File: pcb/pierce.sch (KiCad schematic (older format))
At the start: 49 parts, among them J3 Trackpoint, SW1 SW_PUSH, SW10 SW_PUSH, SW14 SW_PUSH, SW18 SW_PUSH, SW2 SW_PUSH, SW22 SW_PUSH, SW26 SW_PUSH, SW3 SW_PUSH, SW33 SW_PUSH, SW37 SW_PUSH, SW4 SW_PUSH, SW5 SW_PUSH, SW6 SW_PUSH, SW7 SW_PUSH, SW8 SW_PUSH, SW9 SW_PUSH, U1 Elite-C_reverse

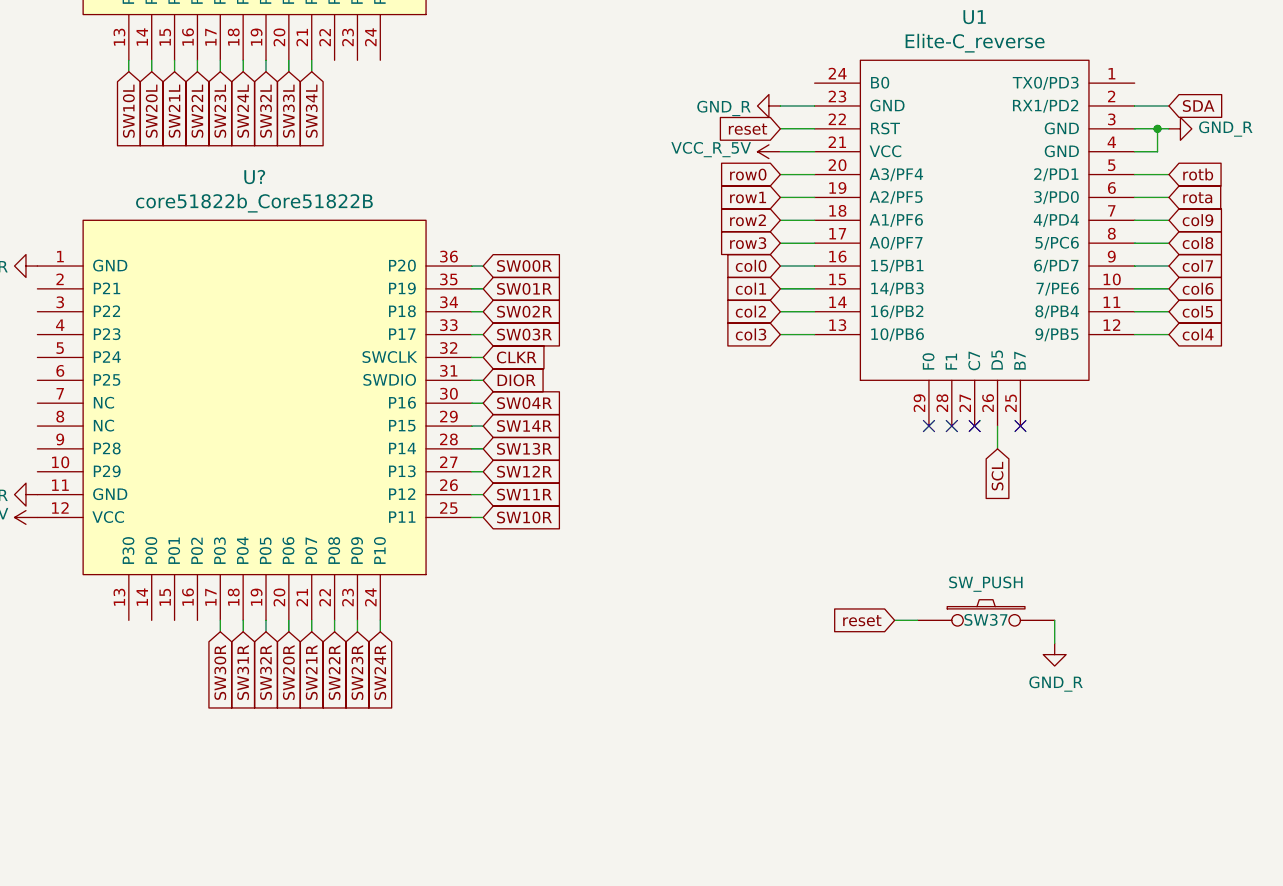
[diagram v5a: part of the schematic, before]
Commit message: adjust schematics with i2c connecion to elite-c
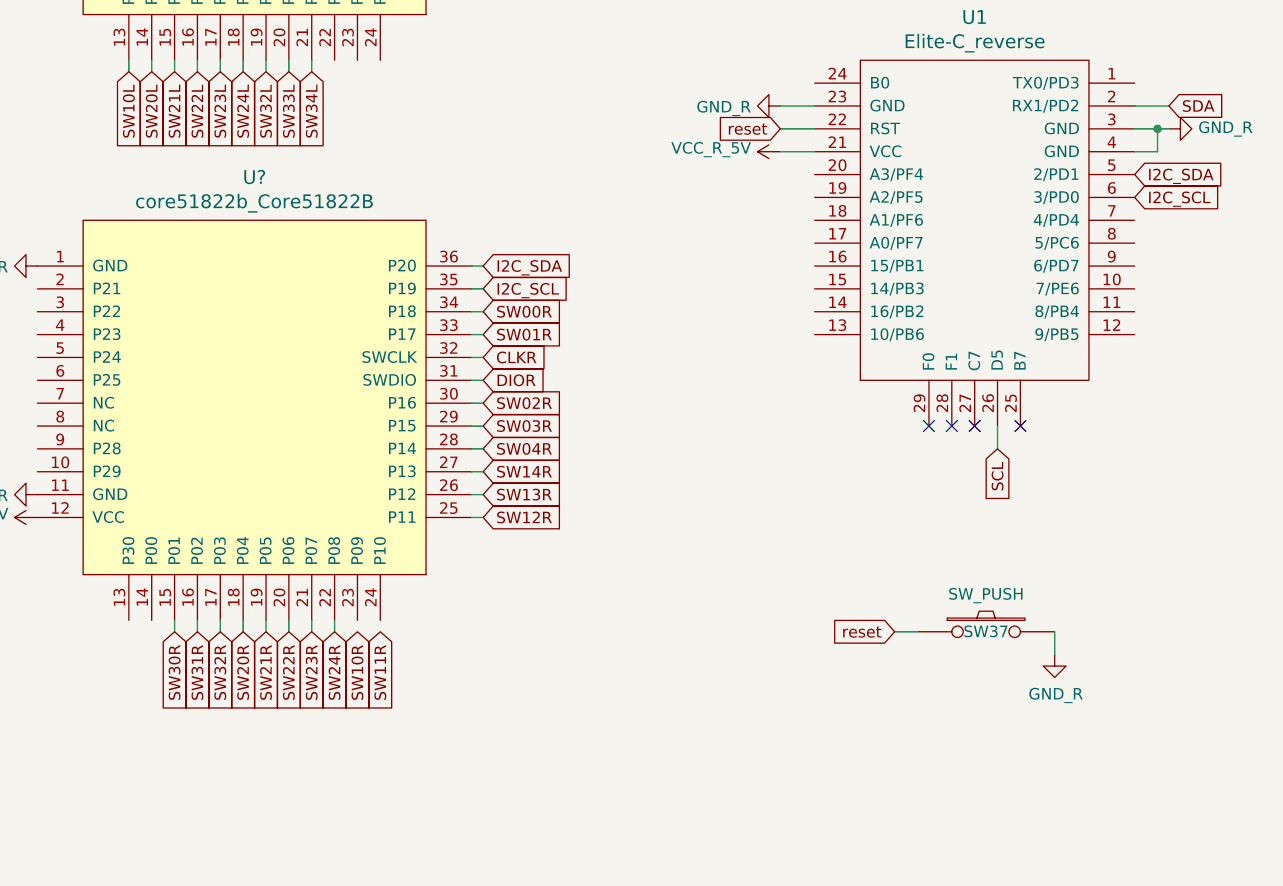
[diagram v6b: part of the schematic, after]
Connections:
- net SW00R: now also U?.34 (P18); no longer U?.36 (P20)
- net SW01R: now also U?.33 (P17); no longer U?.35 (P19)
- net SW02R: now also U?.30 (P16); no longer U?.34 (P18)
- net SW03R: now also U?.29 (P15); no longer U?.33 (P17)
- net SW04R: now also U?.28 (P14); no longer U?.30 (P16)
- net SW10R: no longer U?.25 (P11)
- net SW11R: no longer U?.26 (P12)
- net SW12R: now also U?.25 (P11); no longer U?.27 (P13)
- net SW13R: now also U?.26 (P12); no longer U?.28 (P14)
- net SW14R: now also U?.27 (P13); no longer U?.29 (P15)
- net SW20R: now also U?.18 (P04); no longer U?.20 (P06)
- net SW21R: now also U?.19 (P05); no longer U?.21 (P07)
- net SW22R: now also U?.20 (P06); no longer U?.22 (P08)
- net SW23R: now also U?.21 (P07); no longer U?.23 (P09)
- net SW24R: now also U?.22 (P08); no longer U?.24 (P10)
- net SW30R: now also U?.15 (P01); no longer U?.17 (P03)
- net SW31R: now also U?.16 (P02); no longer U?.18 (P04)
- net SW32R: now also U?.17 (P03); no longer U?.19 (P05)
- net col0: no longer names the net of U1.16 (15/PB1)
- net col1: no longer names the net of U1.15 (14/PB3)
- net col2: no longer names the net of U1.14 (16/PB2)
- net col3: no longer names the net of U1.13 (10/PB6)
- net col4: no longer names the net of U1.12 (9/PB5)
- net col5: no longer names the net of U1.11 (8/PB4)
- net col6: no longer names the net of U1.10 (7/PE6)
- net col7: no longer names the net of U1.9 (6/PD7)
- net col8: no longer names the net of U1.8 (5/PC6)
- net col9: no longer names the net of U1.7 (4/PD4)
- net rota renamed I2C_SCL
- net I2C_SCL: now also U?.35 (P19)
- net rotb renamed I2C_SDA
- net I2C_SDA: now also U?.36 (P20)
- net row0: no longer names the net of U1.20 (A3/PF4)
- net row1: no longer names the net of U1.19 (A2/PF5)
- net row2: no longer names the net of U1.18 (A1/PF6)
- net row3: no longer names the net of U1.17 (A0/PF7)
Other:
- moved on the sheet: SW37
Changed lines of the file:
@@
 Wire Wire Line
 	10700 3250 10750 3250
-Text GLabel 10750 4150 2    50   Input ~ 0
-col4
-Text GLabel 10750 4050 2    50   Input ~ 0
-col5
-Text GLabel 10750 3950 2    50   Input ~ 0
-col6
-Text GLabel 10750 3850 2    50   Input ~ 0
-col7
-Text GLabel 10750 3750 2    50   Input ~ 0
-col8
-Text GLabel 10750 3650 2    50   Input ~ 0
-col9
-Wire Wire Line
-	10600 3650 10750 3650
-Wire Wire Line
-	10600 3750 10750 3750
-Wire Wire Line
-	10600 3850 10750 3850
-Wire Wire Line
-	10600 3950 10750 3950
-Wire Wire Line
-	10600 4050 10750 4050
-Wire Wire Line
-	10600 4150 10750 4150
-$Comp
-L pierce:SW_PUSH SW37
-U 1 1 60617B11
-P 9950 5400
-F 0 "SW37" H 9950 5400 50  0000 C CNN
-F 1 "SW_PUSH" H 9950 5564 50  0000 C CNN
-F 2 "kbd:ResetSW_1side" H 9950 5400 50  0001 C CNN
-F 3 "" H 9950 5400 50  0000 C CNN
-	1    9950 5400
-	1    0    0    -1
-$EndComp
-Text GLabel 9550 5400 0    50   Input ~ 0
-reset
-Wire Wire Line
-	9550 5400 9650 5400
-Wire Wire Line
-	10250 5500 10250 5400
 $Comp
 L Device:R R2
@@
 Wire Wire Line
 	9200 3250 9050 3250
-Text GLabel 9050 3450 0    50   Input ~ 0
-row0
-Text GLabel 9050 3550 0    50   Input ~ 0
-row1
-Text GLabel 9050 3650 0    50   Input ~ 0
-row2
-Text GLabel 9050 3750 0    50   Input ~ 0
-row3
-Text GLabel 9050 3850 0    50   Input ~ 0
-col0
-Text GLabel 9050 3950 0    50   Input ~ 0
-col1
-Text GLabel 9050 4050 0    50   Input ~ 0
-col2
-Text GLabel 9050 4150 0    50   Input ~ 0
-col3
-Wire Wire Line
-	9050 3450 9200 3450
-Wire Wire Line
-	9050 3550 9200 3550
-Wire Wire Line
-	9050 3650 9200 3650
-Wire Wire Line
-	9050 3750 9200 3750
-Wire Wire Line
-	9050 3850 9200 3850
-Wire Wire Line
-	9050 3950 9200 3950
-Wire Wire Line
-	9050 4050 9200 4050
-Wire Wire Line
-	9050 4150 9200 4150
 Wire Wire Line
 	9200 3350 9050 3350
@@
 Wire Wire Line
 	9500 1250 9500 1900
-Text GLabel 10750 3550 2    50   Input ~ 0
-rota
-Text GLabel 10750 3450 2    50   Input ~ 0
-rotb
-Wire Wire Line
-	10750 3450 10600 3450
-Wire Wire Line
-	10750 3550 10600 3550
 $Comp
 L pierce:SW_PUSH SW22
@@
 Wire Wire Line
 	5100 5100 5100 5150
-Text GLabel 7750 3850 2    50   Input ~ 0
+Text GLabel 7750 4050 2    50   Input ~ 0
 SW00R
-Text GLabel 7750 3950 2    50   Input ~ 0
+Text GLabel 7750 4150 2    50   Input ~ 0
 SW01R
-Text GLabel 7750 4050 2    50   Input ~ 0
+Text GLabel 7750 4450 2    50   Input ~ 0
 SW02R
-Text GLabel 7750 4150 2    50   Input ~ 0
+Text GLabel 7750 4550 2    50   Input ~ 0
 SW03R
-Text GLabel 7750 4450 2    50   Input ~ 0
+Text GLabel 7750 4650 2    50   Input ~ 0
 SW04R
-Text GLabel 7750 4550 2    50   Input ~ 0
+Text GLabel 7750 4750 2    50   Input ~ 0
 SW14R
-Text GLabel 7750 4650 2    50   Input ~ 0
+Text GLabel 7750 4850 2    50   Input ~ 0
 SW13R
-Text GLabel 7750 4750 2    50   Input ~ 0
+Text GLabel 7750 4950 2    50   Input ~ 0
 SW12R
-Text GLabel 7750 4850 2    50   Input ~ 0
+Text GLabel 7300 5450 3    50   Input ~ 0
 SW11R
-Text GLabel 7750 4950 2    50   Input ~ 0
+Text GLabel 7200 5450 3    50   Input ~ 0
 SW10R
-Text GLabel 7300 5450 3    50   Input ~ 0
+Text GLabel 7100 5450 3    50   Input ~ 0
 SW24R
-Text GLabel 7200 5450 3    50   Input ~ 0
+Text GLabel 7000 5450 3    50   Input ~ 0
 SW23R
-Text GLabel 7100 5450 3    50   Input ~ 0
+Text GLabel 6900 5450 3    50   Input ~ 0
 SW22R
-Text GLabel 7000 5450 3    50   Input ~ 0
+Text GLabel 6800 5450 3    50   Input ~ 0
 SW21R
-Text GLabel 6900 5450 3    50   Input ~ 0
+Text GLabel 6700 5450 3    50   Input ~ 0
 SW20R
-Text GLabel 6800 5450 3    50   Input ~ 0
+Text GLabel 6600 5450 3    50   Input ~ 0
 SW32R
-Text GLabel 6700 5450 3    50   Input ~ 0
+Text GLabel 6500 5450 3    50   Input ~ 0
 SW31R
-Text GLabel 6600 5450 3    50   Input ~ 0
+Text GLabel 6400 5450 3    50   Input ~ 0
 SW30R
 Wire Wire Line
@@
 	7750 4950 7700 4950
 Wire Wire Line
-	7300 5450 7300 5400
-Wire Wire Line
-	7200 5400 7200 5450
-Wire Wire Line
 	7100 5450 7100 5400
 Wire Wire Line
@@
 Wire Wire Line
 	6600 5400 6600 5450
+Wire Wire Line
+	6500 5450 6500 5400
+Wire Wire Line
+	6400 5400 6400 5450
 Text GLabel 7750 4250 2    50   Input ~ 0
 CLKR
@@
 	0    -1   -1   0
 $EndComp
-$Comp
-L pierce:GND_R #PWR?
-U 1 1 60F94787
-P 10250 5500
-F 0 "#PWR?" H 10250 5250 50  0001 C CNN
-F 1 "GND_R" H 10255 5327 50  0000 C CNN
-F 2 "" H 10250 5500 50  0001 C CNN
-F 3 "" H 10250 5500 50  0001 C CNN
-	1    10250 5500
-	1    0    0    -1
-$EndComp
 Wire Wire Line
 	2750 6800 2750 6750
@@
 	1    0    0    -1
 $EndComp
+Text GLabel 7750 3850 2    50   Input ~ 0
+I2C_SDA
+Text GLabel 7750 3950 2    50   Input ~ 0
+I2C_SCL
+Text GLabel 10600 3450 2    50   Input ~ 0
+I2C_SDA
+Text GLabel 10600 3550 2    50   Input ~ 0
+I2C_SCL
+$Comp
+L pierce:GND_R #PWR?
+U 1 1 60F94787
+P 10250 5550
+F 0 "#PWR?" H 10250 5300 50  0001 C CNN
+F 1 "GND_R" H 10255 5377 50  0000 C CNN
+F 2 "" H 10250 5550 50  0001 C CNN
+F 3 "" H 10250 5550 50  0001 C CNN
+	1    10250 5550
+	1    0    0    -1
+$EndComp
+Wire Wire Line
+	10250 5550 10250 5450
+Wire Wire Line
+	9550 5450 9650 5450
+Text GLabel 9550 5450 0    50   Input ~ 0
+reset
+$Comp
+L pierce:SW_PUSH SW37
+U 1 1 60617B11
+P 9950 5450
+F 0 "SW37" H 9950 5450 50  0000 C CNN
+F 1 "SW_PUSH" H 9950 5614 50  0000 C CNN
+F 2 "kbd:ResetSW_1side" H 9950 5450 50  0001 C CNN
+F 3 "" H 9950 5450 50  0000 C CNN
+	1    9950 5450
+	1    0    0    -1
+$EndComp

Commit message: place and route 2.0
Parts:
- added R4, R5: 4k7, pierce:R_SMD_v2, symbol Device:R
- BT1: renamed from BT?; footprint (none) -> pierce:BatteryHolder_Keystone_3034_1x20mm
- PROGL1, PROGR1: renamed from J?; footprint (none) -> pierce:PinHeader_1x04_P2.54mm_Horizontal
- YJL1, YJR1: renamed from U?; value core51822b_Core51822B -> YJ-14015-NRF51822; footprint (none) -> pierce:YJ-14015
- gave numbers to parts that had none: 22
- renumbered U1 to AVR1, SW37 to RST1, J3 to TP1
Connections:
- net GND is gone; now on net GND_R: R1.1
- net VCC is gone; now on net VCC_R_5V: C1.1, R2.1, R3.1
- net CLKL: now also PROGL1.2 (Pin_2); no longer PROGL1.3 (Pin_3)
- net CLKR: now also PROGR1.2 (Pin_2); no longer PROGR1.3 (Pin_3)
- net DIOL: now also PROGL1.3 (Pin_3); no longer PROGL1.2 (Pin_2)
- net DIOR: now also PROGR1.3 (Pin_3); no longer PROGR1.2 (Pin_2)
- net I2C_SCL: now also R4.1
- net I2C_SDA: now also R5.1
- net SW00R: now also YJR1.33 (P17); no longer YJR1.34 (P18)
- net SW01R: now also YJR1.30 (P16); no longer YJR1.33 (P17)
- net SW02R: now also YJR1.29 (P15); no longer YJR1.30 (P16)
- net SW03R: now also YJR1.28 (P14); no longer YJR1.29 (P15)
- net SW04R: now also YJR1.27 (P13); no longer YJR1.28 (P14)
- net SW10R: now also YJR1.26 (P12)
- net SW11R: now also YJR1.25 (P11)
- net SW12R: now also YJR1.23 (P09); no longer YJR1.25 (P11)
- net SW13R: now also YJR1.24 (P10); no longer YJR1.26 (P12)
- net SW14R: now also YJR1.22 (P08); no longer YJR1.27 (P13)
- net SW20R: now also YJR1.17 (P03); no longer YJR1.18 (P04)
- net SW21R: now also YJR1.18 (P04); no longer YJR1.19 (P05)
- net SW22R: now also YJR1.19 (P05); no longer YJR1.20 (P06)
- net SW23R: now also YJR1.20 (P06); no longer YJR1.21 (P07)
- net SW24R: now also YJR1.21 (P07); no longer YJR1.22 (P08)
- net SW30R: now also YJR1.14 (P00); no longer YJR1.15 (P01)
- net SW32R: now also YJR1.15 (P01); no longer YJR1.17 (P03)
- net VCC_L: now also YJL1.12 (VCC)
- net VCC_R_3.3V: now also R4.2, R5.2
- no-connect marks 4 -> 33
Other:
- moved on the sheet: AVR1, BT1, C1, PROGL1, PROGR1, R1, R2, R3, REG1, RST1, TP1
